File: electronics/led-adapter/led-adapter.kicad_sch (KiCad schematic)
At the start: 18 parts, among them J1 PH2.0 12-pin, J2 PH2.0 12-pin, J3 HUB75, J4 5V in, Q1 2N7002, U1 74AHCT245, U2 74AHCT245

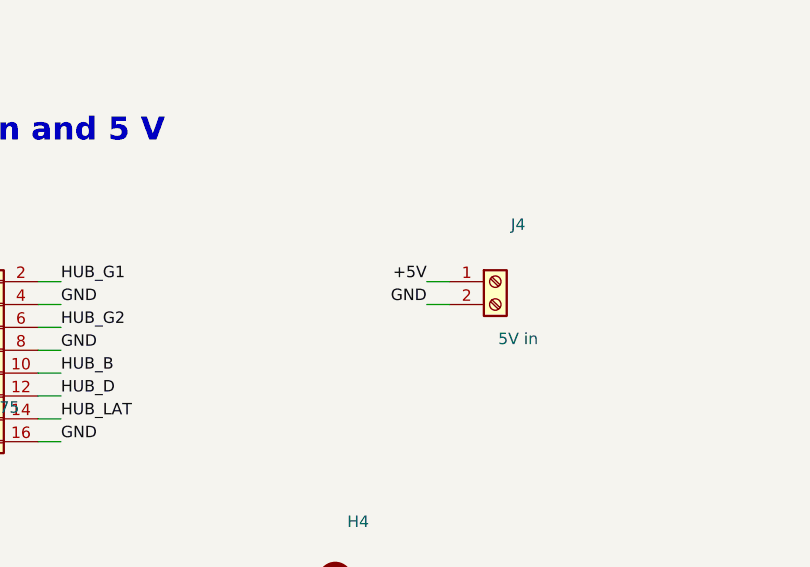
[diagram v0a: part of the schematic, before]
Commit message: Turn the LED adapter's J4 so its wire entries face the front edge
The case expects the 5 V wires to enter J4 from the board's front edge
(ADAPTER_WIRE_KEEPOUT), but the footprint had its openings facing the
board's interior. JLCPCB's preview of revision 1 showed the same, and they
were asked to turn it by hand.

J4 is rotated 180 degrees about its pin line and its pin numbers swap, so
+5V and GND keep the same holes and the copper is unchanged apart from the
square pin-1 pad. Rebuilding from board.json reproduces the placement.

Co-Authored-By: Claude Opus 5.5 <noreply@anthropic.com>
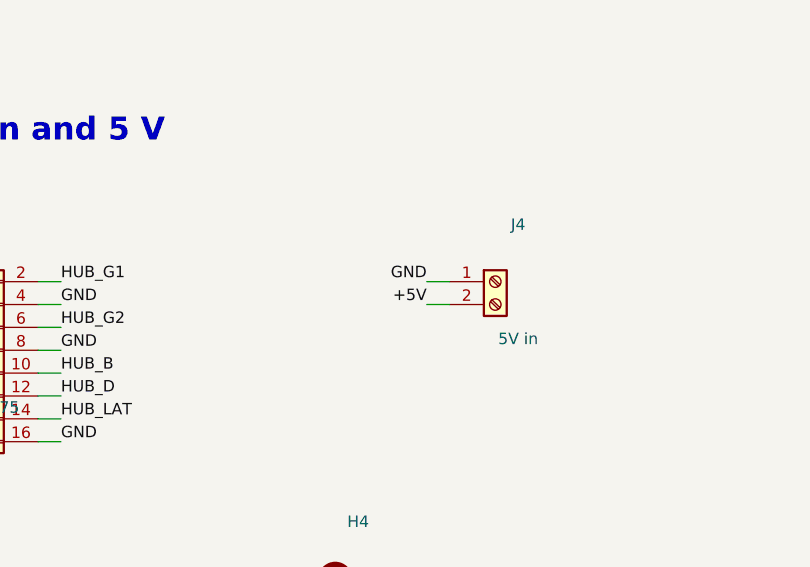
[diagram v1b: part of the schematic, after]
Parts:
- J4: Note From the LED panel's 5 V supply; the buffers draw a few mA. -> From the LED panel's 5 V supply; the buffers draw a few mA.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
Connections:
- net +5V: now also J4.2 (Pin_2); no longer J4.1 (Pin_1)
- net GND: now also J4.1 (Pin_1); no longer J4.2 (Pin_2)
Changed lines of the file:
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@@
 			)
 		)
-		(property "Note" "From the LED panel's 5 V supply; the buffers draw a few mA."
+		(property "Note" "From the LED panel's 5 V supply; the buffers draw a few mA. Wire entries face the board's front edge."
 			(at 411.48 215.9 0)
 			(effects
@@
 		)
 	)
-	(label "+5V"
+	(label "GND"
 		(at 403.86 215.9 180)
 		(effects
@@
 		)
 	)
-	(label "GND"
+	(label "+5V"
 		(at 403.86 218.44 180)
 		(effects
